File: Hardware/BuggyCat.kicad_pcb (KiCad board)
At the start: 2 copper layers, 36.8 x 104 mm, 76 parts, among them J1 Antenna, J2 BG306-02-A-2-0400-L-G, J3 Header7, J4 Header 2, J5 Header 4, J6 Input Power:2x AA Battery, P1 USB_C_Plug_USB2.0, Q1 AO3422, Q2 AO3422, Q3 LDA111STR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

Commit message: Reassigned footprints and 3d models
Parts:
- C4: footprint chipshouter:CAPC6153X500N -> BuggyCat:CAPC6153X500N
- J1: footprint chipshouter:732511150 -> BuggyCat:732511150
- J2: footprint chipshouter:BG30602A20400LG -> BuggyCat:BG30602A20400LG
- J6: footprint chipshouter:JST_S2B-PH-K-S(LF)(SN) -> BuggyCat:JST_S2B-PH-K-S(LF)(SN)
- Q3: footprint chipshouter:SOP254P952X470-6N -> BuggyCat:SOP254P952X470-6N
- R11: footprint chipshouter:RESC6432X120N -> BuggyCat:RESC6432X120N
- T1, T2: footprint chipshouter:ATB3225240110T000 -> BuggyCat:ATB3225240110T000
- U2: footprint chipshouter:W25Q16JVUUIQ -> BuggyCat:W25Q16JVUUIQ
- U3: footprint chipshouter:RP2040-QFN-56 -> BuggyCat:RP2040-QFN-56

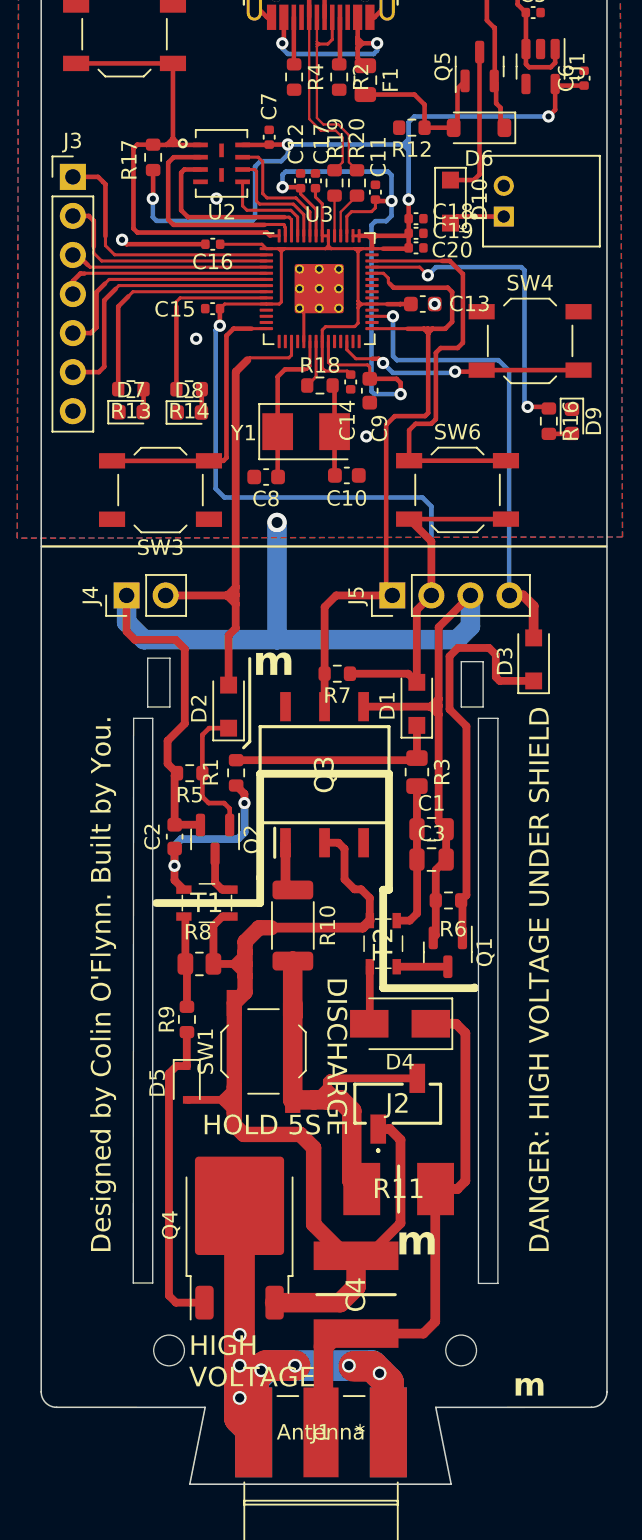
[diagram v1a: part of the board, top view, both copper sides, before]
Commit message: Change routing of PCB
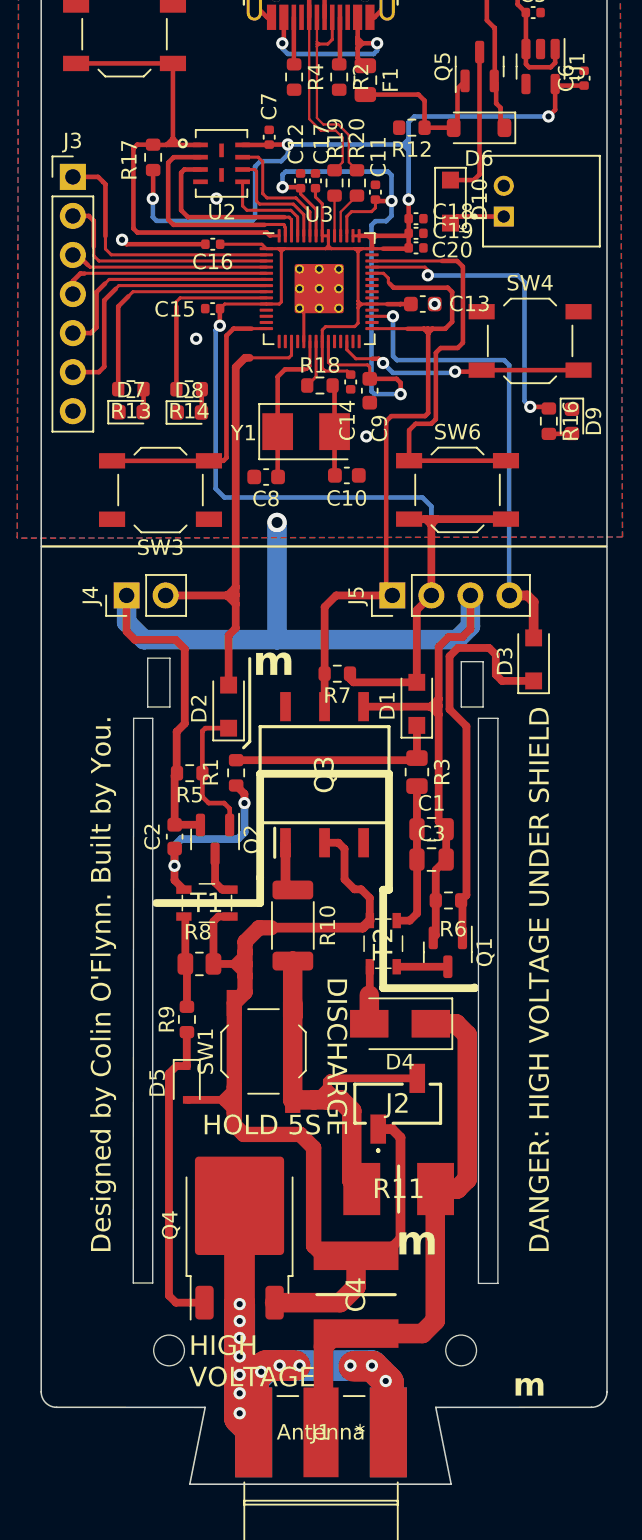
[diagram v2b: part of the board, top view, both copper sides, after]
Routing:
- net Net-(J1-Ext): track 50.8 -> 52.9 mm, vias 7 -> 13
- net Net-(D5-A): track 74.6 -> 76.2 mm
- net /GP27: track 20.8 -> 20.0 mm
- net +3V3: track 151.9 -> 152.5 mm

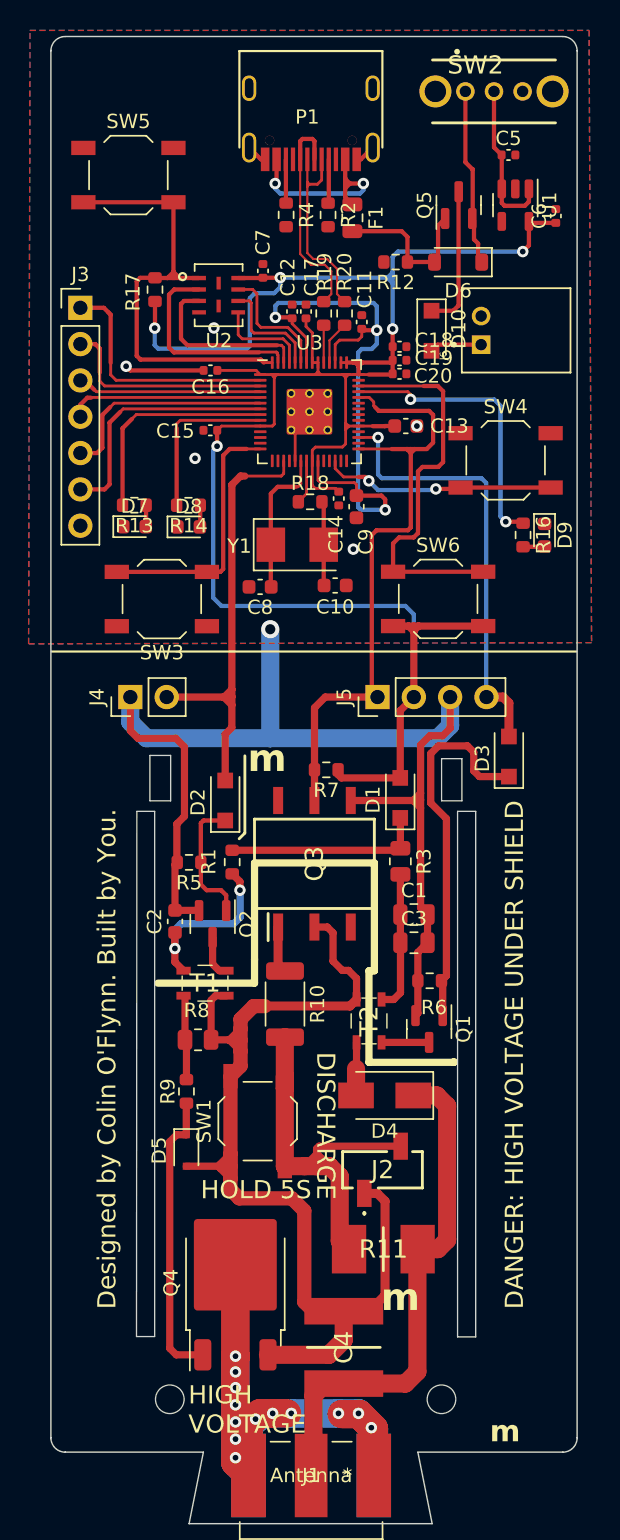
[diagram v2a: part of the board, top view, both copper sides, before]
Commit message: Update logos
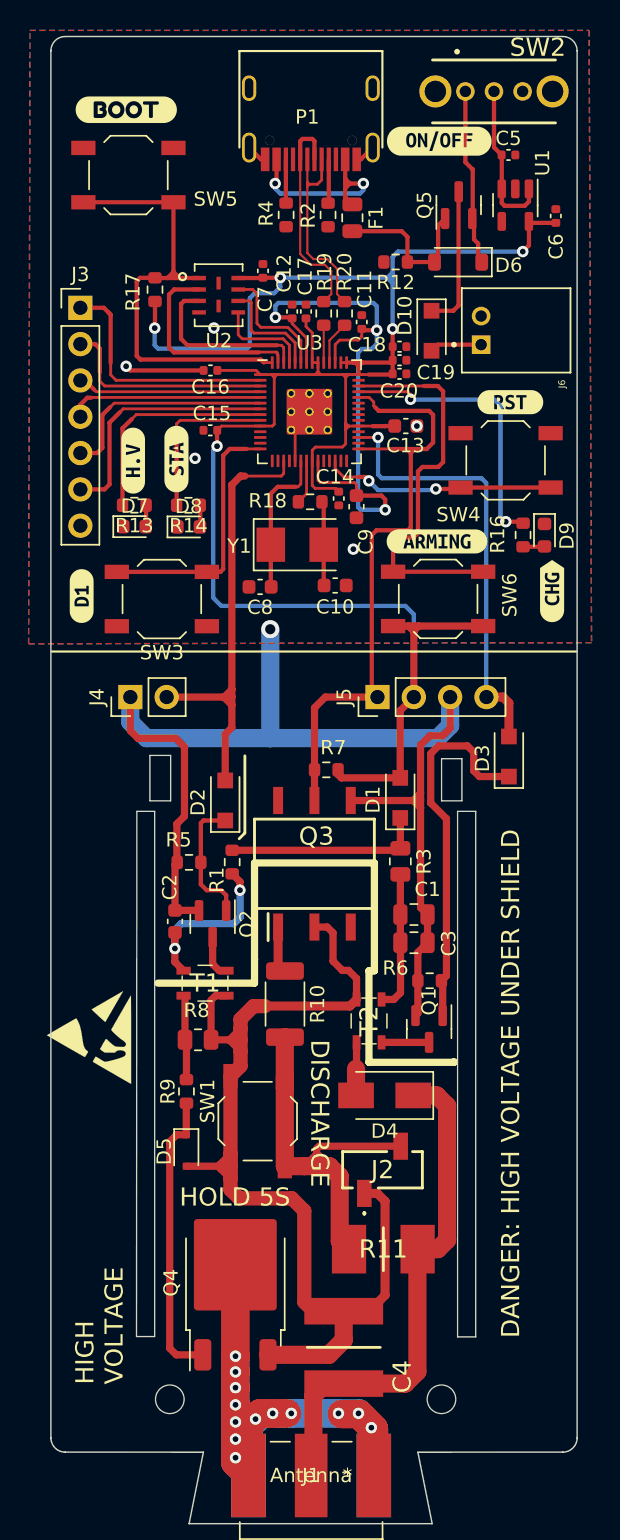
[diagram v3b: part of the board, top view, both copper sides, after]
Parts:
- added G***: LOGO, calderon_7.5x7.5, B.Cu at (65.3, 82.8)
- added G***: LOGO, Symbol_EC:electronic_cats_logo_8x6, B.Cu at (66.3, 39.3)
- added REF**: ESD-Logo_6.6x6mm_SilkScreen, Symbol:ESD-Logo_6.6x6mm_SilkScreen, F.Cu at (50.5, 89.8)
- added REF**: OSHW-Logo_7.5x8mm_SilkScreen, Symbol:OSHW-Logo_7.5x8mm_SilkScreen, B.Cu at (65.0, 92.0)
- added kibuzzard-642DF578: G***, kibuzzard-642DF578, F.Cu at (80.0, 45.4)
- added kibuzzard-642DF5C4: G***, kibuzzard-642DF5C4, F.Cu at (53.2, 24.9)
- added kibuzzard-642DF6A9: G***, kibuzzard-642DF6A9, F.Cu at (53.6, 49.5)
- added kibuzzard-642DF6E0: G***, kibuzzard-642DF6E0, F.Cu at (56.7, 49.4)
- added kibuzzard-642DF726: G***, kibuzzard-642DF726, F.Cu at (82.9, 58.6)
- added kibuzzard-642DF795: G***, kibuzzard-642DF795, F.Cu at (50.0, 58.9)
- added kibuzzard-642DF7A2: G***, kibuzzard-642DF7A2, B.Cu at (53.6, 41.2)
- added kibuzzard-642DF7B5: G***, kibuzzard-642DF7B5, B.Cu at (53.6, 38.8)
- added kibuzzard-642DF7CA: G***, kibuzzard-642DF7CA, B.Cu at (53.7, 44.0)
- added kibuzzard-642DF7D8: G***, kibuzzard-642DF7D8, B.Cu at (53.6, 46.5)
- added kibuzzard-642DF7E6: G***, kibuzzard-642DF7E6, B.Cu at (53.7, 48.7)
- added kibuzzard-642DF805: G***, kibuzzard-642DF805, B.Cu at (53.4, 54.1)
- added kibuzzard-642DF817: G***, kibuzzard-642DF817, B.Cu at (53.7, 51.3)
- added kibuzzard-642DF8F6: G***, kibuzzard-642DF8F6, F.Cu at (75.0, 27.1)
- added kibuzzard-642E0AC9: G***, kibuzzard-642E0AC9, B.Cu at (55.9, 60.1)
- added kibuzzard-642E0AD5: G***, kibuzzard-642E0AD5, B.Cu at (53.3, 61.6)
- added kibuzzard-642E0AF5: G***, kibuzzard-642E0AF5, B.Cu at (78.3, 60.9)
- added kibuzzard-642E0B26: G***, kibuzzard-642E0B26, B.Cu at (75.8, 61.7)
- added kibuzzard-642E0B82: G***, kibuzzard-642E0B82, B.Cu at (73.2, 61.6)
- added kibuzzard-642E0B91: G***, kibuzzard-642E0B91, B.Cu at (70.6, 60.1)
- added kibuzzard-642E0E1B: G***, kibuzzard-642E0E1B, B.Cu at (66.0, 46.0)
- added kibuzzard-642E0E2F: G***, kibuzzard-642E0E2F, B.Cu at (65.9, 50.1)
- added kibuzzard-642E0F9F: G***, kibuzzard-642E0F9F, B.Cu at (68.9, 78.0)
- added kibuzzard-642E11AF: G***, kibuzzard-642E11AF, F.Cu at (74.9, 55.1)
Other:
- board text removed: "Designed by Colin O'Flynn. Built by You."

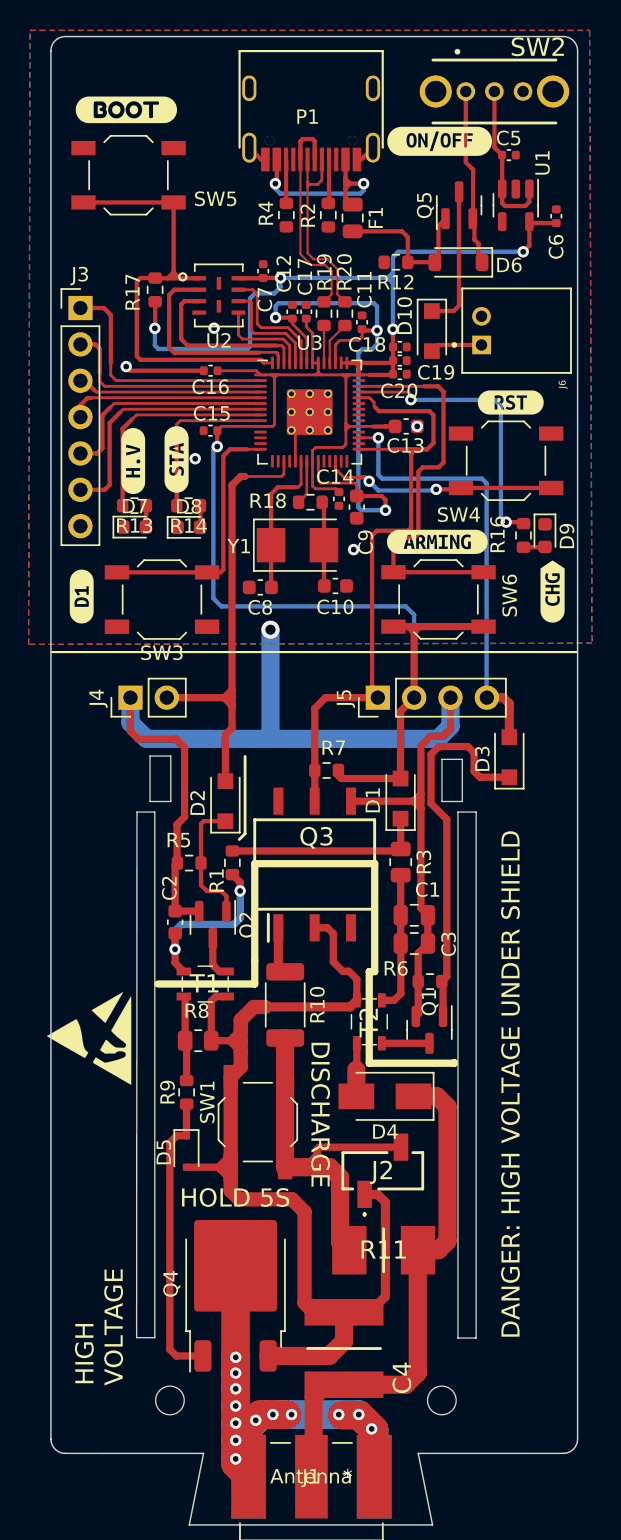
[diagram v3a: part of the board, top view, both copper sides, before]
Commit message: Rounded PCB corners
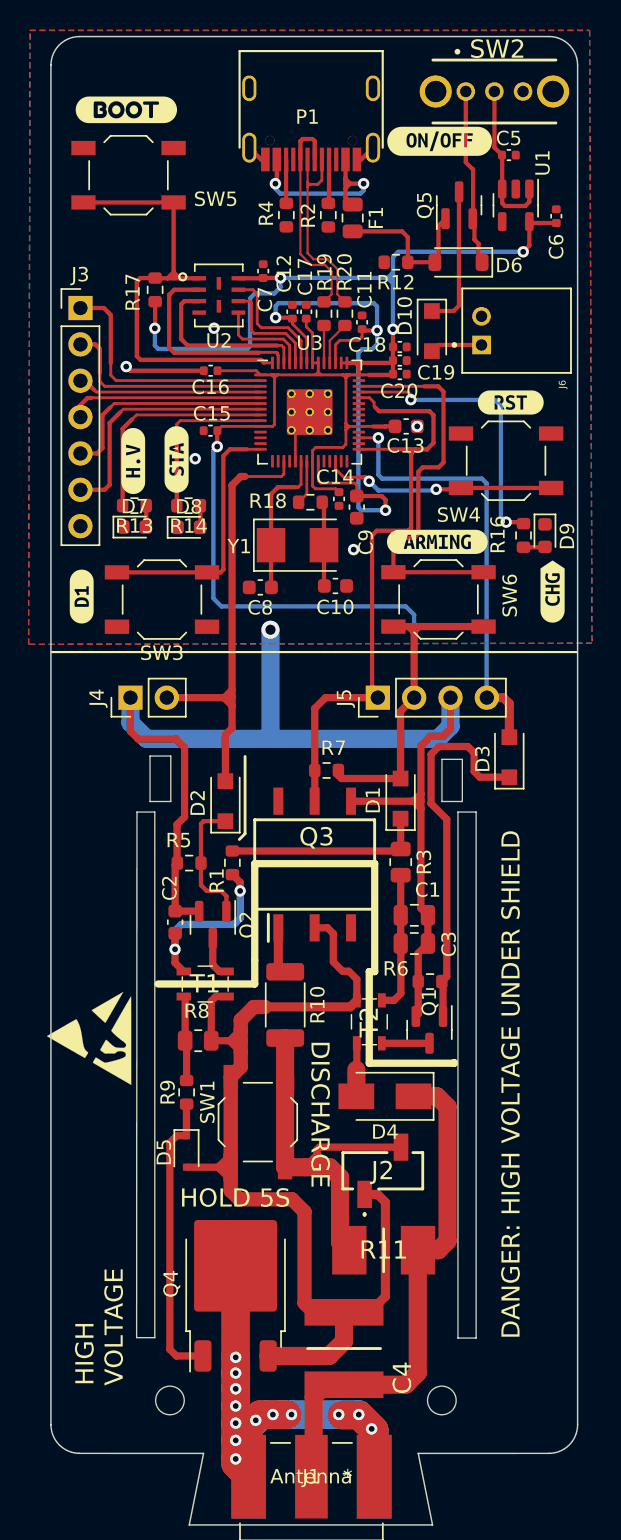
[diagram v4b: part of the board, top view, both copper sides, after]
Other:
- outline, holes or cut-outs redrawn
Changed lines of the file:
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@@
     (property "ki_keywords" "switch lever")
     (attr through_hole)
-    (fp_text reference "SW2" (at 3.0625 -3.07986) (layer "F.SilkS")
+    (fp_text reference "SW2" (at 0.2225 -2.94986) (layer "F.SilkS")
         (effects (font (size 1.27 1.27) (thickness 0.254)))
     )
@@
     (attr board_only exclude_from_pos_files exclude_from_bom)
     (fp_text reference "kibuzzard-642E11AF" (at 0 -3.891492) (layer "F.SilkS") hide
-        (effects (font (size 0 0)))
+        (effects (font (size 0 0) (thickness 0.15)))
     )
     (fp_text value "G***" (at 0 3.891492) (layer "F.SilkS") hide
-        (effects (font (size 0 0)))
+        (effects (font (size 0 0) (thickness 0.15)))
     )
     (fp_poly
@@
   (gr_line (start 75.2118 70.3142) (end 75.2118 73.2606)
     (stroke (width 0.05) (type solid)) (layer "Edge.Cuts"))
-  (gr_line (start 47.89 20.81) (end 47.89 117.81)
+  (gr_line (start 47.89 21.81) (end 47.89 116.81)
     (stroke (width 0.1) (type default)) (layer "Edge.Cuts"))
-  (gr_line (start 73.5544 118.8134) (end 83.69 118.81)
+  (gr_line (start 73.5544 118.8134) (end 82.69 118.81)
     (stroke (width 0.1) (type default)) (layer "Edge.Cuts"))
-  (gr_arc (start 48.89 118.81) (mid 48.182893 118.517107) (end 47.89 117.81)
+  (gr_arc (start 49.89 118.808236) (mid 48.476153 118.223331) (end 47.890001 116.81)
     (stroke (width 0.1) (type default)) (layer "Edge.Cuts"))
   (gr_line (start 53.9012 73.9972) (end 55.1458 73.9972)
@@
   (gr_line (start 77.5994 73.9972) (end 76.3294 73.9972)
     (stroke (width 0.05) (type solid)) (layer "Edge.Cuts"))
-  (gr_arc (start 83.69 19.81) (mid 84.397107 20.102893) (end 84.69 20.81)
+  (gr_arc (start 82.699407 19.807621) (mid 84.109409 20.396545) (end 84.689999 21.81)
     (stroke (width 0.1) (type default)) (layer "Edge.Cuts"))
   (gr_line (start 77.5994 110.751) (end 77.5994 73.9972)
@@
   (gr_line (start 55.1458 73.9972) (end 55.1458 110.7256)
     (stroke (width 0.05) (type solid)) (layer "Edge.Cuts"))
-  (gr_line (start 48.89 19.81) (end 83.69 19.81)
+  (gr_line (start 49.89 19.81) (end 82.69 19.81)
     (stroke (width 0.1) (type default)) (layer "Edge.Cuts"))
   (gr_line (start 55.1458 110.7256) (end 53.8758 110.7256)
@@
   (gr_line (start 74.5544 123.8134) (end 57.5544 123.8134)
     (stroke (width 0.1) (type default)) (layer "Edge.Cuts"))
-  (gr_arc (start 84.69 117.81) (mid 84.397107 118.517107) (end 83.69 118.81)
+  (gr_arc (start 84.69 116.81) (mid 84.104214 118.224214) (end 82.69 118.81)
     (stroke (width 0.1) (type default)) (layer "Edge.Cuts"))
   (gr_line (start 57.5544 123.8134) (end 58.5544 118.8134)
@@
   (gr_line (start 54.8156 73.2606) (end 54.8156 70.0856)
     (stroke (width 0.05) (type solid)) (layer "Edge.Cuts"))
-  (gr_arc (start 47.89 20.81) (mid 48.182893 20.102893) (end 48.89 19.81)
+  (gr_arc (start 47.89 21.81) (mid 48.475786 20.395786) (end 49.89 19.81)
     (stroke (width 0.1) (type default)) (layer "Edge.Cuts"))
   (gr_line (start 76.6342 73.2606) (end 76.6342 70.3142)
     (stroke (width 0.05) (type solid)) (layer "Edge.Cuts"))
-  (gr_line (start 58.5544 118.8134) (end 48.89 118.81)
+  (gr_line (start 58.5544 118.8134) (end 49.89 118.81)
     (stroke (width 0.1) (type default)) (layer "Edge.Cuts"))
   (gr_line (start 76.6342 70.3142) (end 75.2118 70.3142)
@@
   (gr_line (start 56.2634 70.0856) (end 56.2634 73.2606)
     (stroke (width 0.05) (type solid)) (layer "Edge.Cuts"))
-  (gr_line (start 84.69 20.81) (end 84.69 117.81)
+  (gr_line (start 84.69 21.81) (end 84.69 116.81)
     (stroke (width 0.1) (type default)) (layer "Edge.Cuts"))
   (gr_line (start 73.5544 118.8134) (end 74.5544 123.8134)

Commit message: change label pulse
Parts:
- removed kibuzzard-642DF795: G***, kibuzzard-642DF795
- added kibuzzard-642F0B74: G***, kibuzzard-642F0B74, F.Cu at (50.0, 58.9)
